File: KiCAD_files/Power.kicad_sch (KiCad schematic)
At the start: 44 parts, among them J101 Wago 6 contacts, P101 Power2, U101 AMC1311, U102 MCP6486UT-E/LT, U103 MCP6486UT-E/LT, U104 ACS723LLCTR-20AB

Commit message: modified some functions and subfunctions
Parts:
- C101, C102, C103, C106, C117, C119, C123, C124, R103, R104, R105, R107, R110, R111, R115, R116, R117, R118, U101, U102, U103, U104: Functional Block Measurment -> Measurement
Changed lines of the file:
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@@
       (effects (font (size 1.27 1.27)) hide)
     )
-    (property "Functional Block" "Measurment" (at 215.9 67.31 0)
+    (property "Functional Block" "Measurement" (at 215.9 67.31 0)
       (effects (font (size 1.27 1.27)) hide)
     )
@@
       (effects (font (size 1.27 1.27)) hide)
     )
-    (property "Functional Block" "Measurment" (at 241.3 55.88 0)
+    (property "Functional Block" "Measurement" (at 241.3 55.88 0)
       (effects (font (size 1.27 1.27)) hide)
     )
@@
       (effects (font (size 1.27 1.27)) hide)
     )
-    (property "Functional Block" "Measurment" (at 209.55 107.95 0)
+    (property "Functional Block" "Measurement" (at 209.55 107.95 0)
       (effects (font (size 1.27 1.27)) hide)
     )
@@
       (effects (font (size 1.27 1.27)) hide)
     )
-    (property "Functional Block" "Measurment" (at 209.55 128.27 0)
+    (property "Functional Block" "Measurement" (at 209.55 128.27 0)
       (effects (font (size 1.27 1.27)) hide)
     )
@@
       (effects (font (size 1.27 1.27)) hide)
     )
-    (property "Functional Block" "Measurment" (at 85.09 222.25 0)
+    (property "Functional Block" "Measurement" (at 85.09 222.25 0)
       (effects (font (size 1.27 1.27)) hide)
     )
@@
       (effects (font (size 1.27 1.27)) hide)
     )
-    (property "Functional Block" "Measurment" (at 231.14 189.23 0)
+    (property "Functional Block" "Measurement" (at 231.14 189.23 0)
       (effects (font (size 1.27 1.27)) hide)
     )
@@
       (effects (font (size 1.27 1.27)) hide)
     )
-    (property "Functional Block" "Measurment" (at 241.3 213.36 0)
+    (property "Functional Block" "Measurement" (at 241.3 213.36 0)
       (effects (font (size 1.27 1.27)) hide)
     )
@@
       (effects (font (size 1.27 1.27)) hide)
     )
-    (property "Functional Block" "Measurment" (at 217.17 215.9 0)
+    (property "Functional Block" "Measurement" (at 217.17 215.9 0)
       (effects (font (size 1.27 1.27)) hide)
     )
@@
       (effects (font (size 1.27 1.27)) hide)
     )
-    (property "Functional Block" "Measurment" (at 242.57 232.41 0)
+    (property "Functional Block" "Measurement" (at 242.57 232.41 0)
       (effects (font (size 1.27 1.27)) hide)
     )
@@
       (effects (font (size 1.27 1.27)) hide)
     )
-    (property "Functional Block" "Measurment" (at 113.03 217.17 0)
+    (property "Functional Block" "Measurement" (at 113.03 217.17 0)
       (effects (font (size 1.27 1.27)) hide)
     )
@@
       (effects (font (size 1.27 1.27)) hide)
     )
-    (property "Functional Block" "Measurment" (at 113.03 222.25 0)
+    (property "Functional Block" "Measurement" (at 113.03 222.25 0)
       (effects (font (size 1.27 1.27)) hide)
     )
@@
       (effects (font (size 1.27 1.27)) hide)
     )
-    (property "Functional Block" "Measurment" (at 140.97 219.71 0)
+    (property "Functional Block" "Measurement" (at 140.97 219.71 0)
       (effects (font (size 1.27 1.27)) hide)
     )
@@
       (effects (font (size 1.27 1.27)) hide)
     )
-    (property "Functional Block" "Measurment" (at 128.27 212.09 0)
+    (property "Functional Block" "Measurement" (at 128.27 212.09 0)
       (effects (font (size 1.27 1.27)) hide)
     )
@@
       (effects (font (size 1.27 1.27)) hide)
     )
-    (property "Functional Block" "Measurment" (at 140.97 236.22 0)
+    (property "Functional Block" "Measurement" (at 140.97 236.22 0)
       (effects (font (size 1.27 1.27)) hide)
     )
@@
       (effects (font (size 1.27 1.27)) hide)
     )
-    (property "Functional Block" "Measurment" (at 60.96 191.77 0)
+    (property "Functional Block" "Measurement" (at 60.96 191.77 0)
       (effects (font (size 1.27 1.27)) hide)
     )
@@
       (effects (font (size 1.27 1.27)) hide)
     )
-    (property "Functional Block" "Measurment" (at 92.71 193.04 0)
+    (property "Functional Block" "Measurement" (at 92.71 193.04 0)
       (effects (font (size 1.27 1.27)) hide)
     )
@@
       (effects (font (size 1.27 1.27)) hide)
     )
-    (property "Functional Block" "Measurment" (at 231.14 205.74 0)
+    (property "Functional Block" "Measurement" (at 231.14 205.74 0)
       (effects (font (size 1.27 1.27)) hide)
     )
@@
       (effects (font (size 1.27 1.27)) hide)
     )
-    (property "Functional Block" "Measurment" (at 217.17 210.82 0)
+    (property "Functional Block" "Measurement" (at 217.17 210.82 0)
       (effects (font (size 1.27 1.27)) hide)
     )
@@
       (effects (font (size 1.27 1.27)) hide)
     )
-    (property "Functional Block" "Measurment" (at 130.81 191.77 0)
+    (property "Functional Block" "Measurement" (at 130.81 191.77 0)
       (effects (font (size 1.27 1.27)) hide)
     )
@@
       (effects (font (size 1.27 1.27)) hide)
     )
-    (property "Functional Block" "Measurment" (at 241.3 241.3 0)
+    (property "Functional Block" "Measurement" (at 241.3 241.3 0)
       (effects (font (size 1.27 1.27)) hide)
     )
@@
       (effects (font (size 1.27 1.27)) hide)
     )
-    (property "Functional Block" "Measurment" (at 224.79 226.06 0)
+    (property "Functional Block" "Measurement" (at 224.79 226.06 0)
       (effects (font (size 1.27 1.27)) hide)
     )
@@
       (effects (font (size 1.27 1.27)) hide)
     )
-    (property "Functional Block" "Measurment" (at 140.97 245.11 0)
-      (effects (font (size 1.27 1.27)) hide)
-    )
+    (property "Functional Block" "Measurement" (at 140.97 245.11 0)
+      (effects (font (size 1.27 1.27)) hide)
+    )

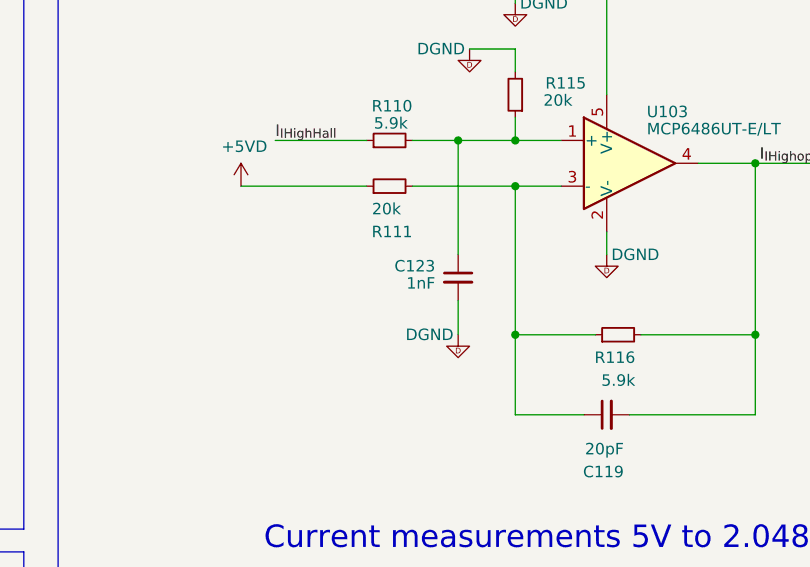
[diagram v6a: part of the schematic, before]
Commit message: cleaned manf and value missmatch
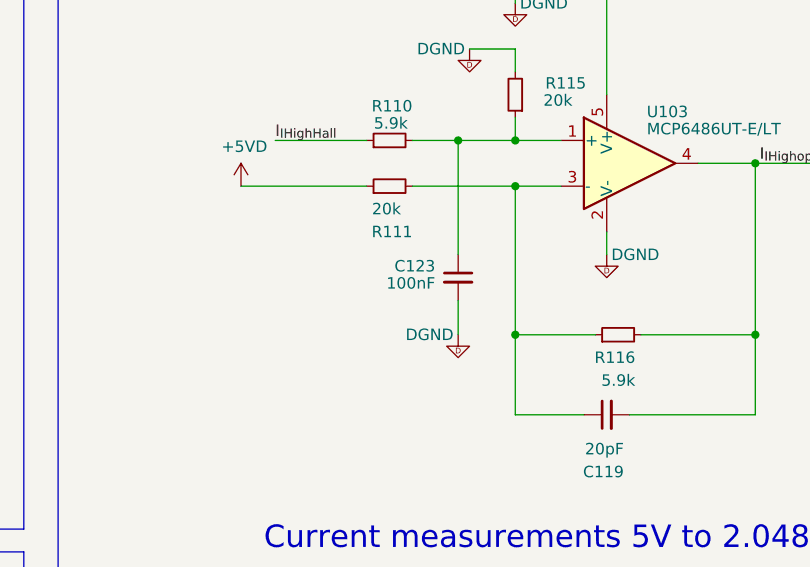
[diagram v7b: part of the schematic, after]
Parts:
- C123: value 1nF -> 100nF
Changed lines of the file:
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@@
       (effects (font (size 1.27 1.27)) (justify left))
     )
-    (property "Value" "1nF" (at 222.25 226.695 0)
+    (property "Value" "100nF" (at 222.25 226.695 0)
       (effects (font (size 1.27 1.27)) (justify left))
     )

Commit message: corrected datasheet links
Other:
- note added: "BW_SEL to VCC for 20kHz BW BW_SEL to GND for 80kHz BW"
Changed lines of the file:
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@@
   )
   (text "https://www.allegromicro.com/en/Insights-and-Innovations/\nTechnical-Documents/Hall-Effect-Sensor-IC-Publications/\nShifting-the-Offset-Voltage-of-Current-Sensors"
-    (at 203.2 274.955 0)
-    (effects (font (size 1.27 1.27)) (justify left bottom))
-  )
-  (text "V_{SHIFTED} = I_{IHigh} - 1.5V\n" (at 203.2 266.954 0)
+    (at 182.88 276.225 0)
+    (effects (font (size 1.27 1.27)) (justify left bottom))
+  )
+  (text "V_{SHIFTED} = I_{IHigh} - 1.5V\n" (at 182.88 268.224 0)
     (effects (font (size 1.27 1.27)) (justify left bottom))
   )
@@
     (effects (font (size 1.27 1.27)) (justify left bottom))
   )
-  (text "High side current sensor" (at 207.01 35.56 0)
+  (text "High side current sensor" (at 207.01 29.21 0)
     (effects (font (size 1.27 1.27)) (justify left bottom))
   )
   (text "V_{SHIFTED} = I_{IHigh} - (5.9k/20k)* 5V_{Digital}"
-    (at 203.073 263.906 0)
+    (at 182.753 265.176 0)
     (effects (font (size 1.27 1.27)) (justify left bottom))
   )
@@
     (effects (font (size 1.2446 1.2446)) (justify left bottom))
   )
+  (text "BW_SEL to VCC for 20kHz BW\nBW_SEL to GND for 80kHz BW"
+    (at 248.92 45.72 0)
+    (effects (font (size 1.27 1.27)) (justify left bottom))
+  )
   (text "Power Leg 1" (at 101.6 85.09 0)
     (effects (font (size 3.5 3.5)) (justify left bottom))
   )
-  (text "High Side Voltage Measure" (at 24.13 173.99 0)
-    (effects (font (size 2.54 2.54)) (justify left bottom))
-  )
-  (text "Current measurements 5V to 2.048\n" (at 203.2 256.54 0)
+  (text "High Side Voltage Measure" (at 22.86 172.72 0)
+    (effects (font (size 2 2)) (justify left bottom))
+  )
+  (text "Current measurements 5V to 2.048\n" (at 182.88 257.81 0)
     (effects (font (size 2.4892 2.4892)) (justify left bottom))
   )
@@
   )
   (text "V_{SHIFTED} = ((R116 + R111)*R115 / (R115 + R110)*R111) * I_{IHigh} - (R116/R111)* 5V_{Digital}"
-    (at 203.2 260.35 0)
+    (at 182.88 261.62 0)
     (effects (font (size 1.27 1.27)) (justify left bottom))
   )
@@
   )
   (text "Mechanical housing \nand heatsink holes" (at 24.13 266.7 0)
-    (effects (font (size 2.54 2.54)) (justify left bottom))
+    (effects (font (size 2 2)) (justify left bottom))
   )
   (text "Low Side \nMax 80V\nMin 9V\n0-16A\n8A max / Leg" (at 96.52 35.56 0)
@@
       (effects (font (size 1.27 1.27)) hide)
     )
-    (property "Datasheet" "http://www.allegromicro.com/~/media/Files/Datasheets/ACS712-Datasheet.ashx?la=en" (at 215.9 67.31 0)
+    (property "Datasheet" "https://www.google.com/url?sa=t&rct=j&q=&esrc=s&source=web&cd=&cad=rja&uact=8&ved=2ahUKEwjikvr_8ZeAAxWDTqQEHfwEAu0QFnoECBEQAQ&url=https%3A%2F%2Fwww.allegromicro.com%2F~%2Fmedia%2Ffiles%2Fdatasheets%2Facs723-datasheet.ashx&usg=AOvVaw2qZ9b_k2ocxzc58dTK1Pl7&opi=89978449" (at 215.9 67.31 0)
       (effects (font (size 1.27 1.27)) hide)
     )
